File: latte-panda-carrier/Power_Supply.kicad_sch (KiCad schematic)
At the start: 0 parts

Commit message: 110.3
USB-C sub-circuit
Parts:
- added C61: 1uF/16V, A_HDJ_Library:C_0402_1005Metric, symbol Device:C_Small
- added D10, D11: ESD9B5.0ST5G, A_HDJ_Library:D_0402_1005Metric, symbol Diode:ESD9B5.0ST5G
- added D12, D13, D14: D_Zener, A_HDJ_Library:D_0402_1005Metric, symbol Device:D_Zener
- added J17: Barrel_Jack_Switch, symbol Connector:Barrel_Jack_Switch
- added J18: USB_C_Receptacle_USB2.0_16P, symbol Connector:USB_C_Receptacle_USB2.0_16P
- added R36: 10K/1%, A_HDJ_Library:R_0402_1005Metric, symbol Device:R
- added R37: 1K/1%, A_HDJ_Library:R_0402_1005Metric, symbol Device:R
- added R43: 56K/1%, A_HDJ_Library:R_0402_1005Metric, symbol Device:R
- added U14: USB PD等快充协议受电芯片-CH224K-ESSOP10, A_HDJ_Library:ESSOP-10-1EP_3.9x5mm_P1.0mm_EP3.2x2.3, symbol latte_hdj:CH224K
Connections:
- new net: D13.1 (K), J18.A5 (CC1), U14.7 (CC1)
- new net: R36.2, U14.8 (VBUS)
- new net: C61.2, R37.2, U14.1 (VDD)
- new net: J18.A6 (D+), J18.B6 (D+), U14.4 (DP)
- new net: D10.2 (A2), D11.2 (A2), J18.A7 (D-), J18.B7 (D-), U14.5 (DM)
- new net: D14.1 (K), J18.B5 (CC2), U14.6 (CC2)
- new net: R43.1, U14.9 (CFG1)
- new net +15V: D12.1 (K), J18.A4 (VBUS), J18.A9 (VBUS), J18.B4 (VBUS), J18.B9 (VBUS), R36.1
- new net GND: C61.1, D10.1 (A1), D11.1 (A1), D12.2 (A), D13.2 (A), D14.2 (A), J18.A1 (GND), J18.A12 (GND), J18.B1 (GND), J18.B12 (GND), J18.S1 (SHIELD), R37.1, R43.2, U14.0 (GND)
- no-connect marks 0 -> 5

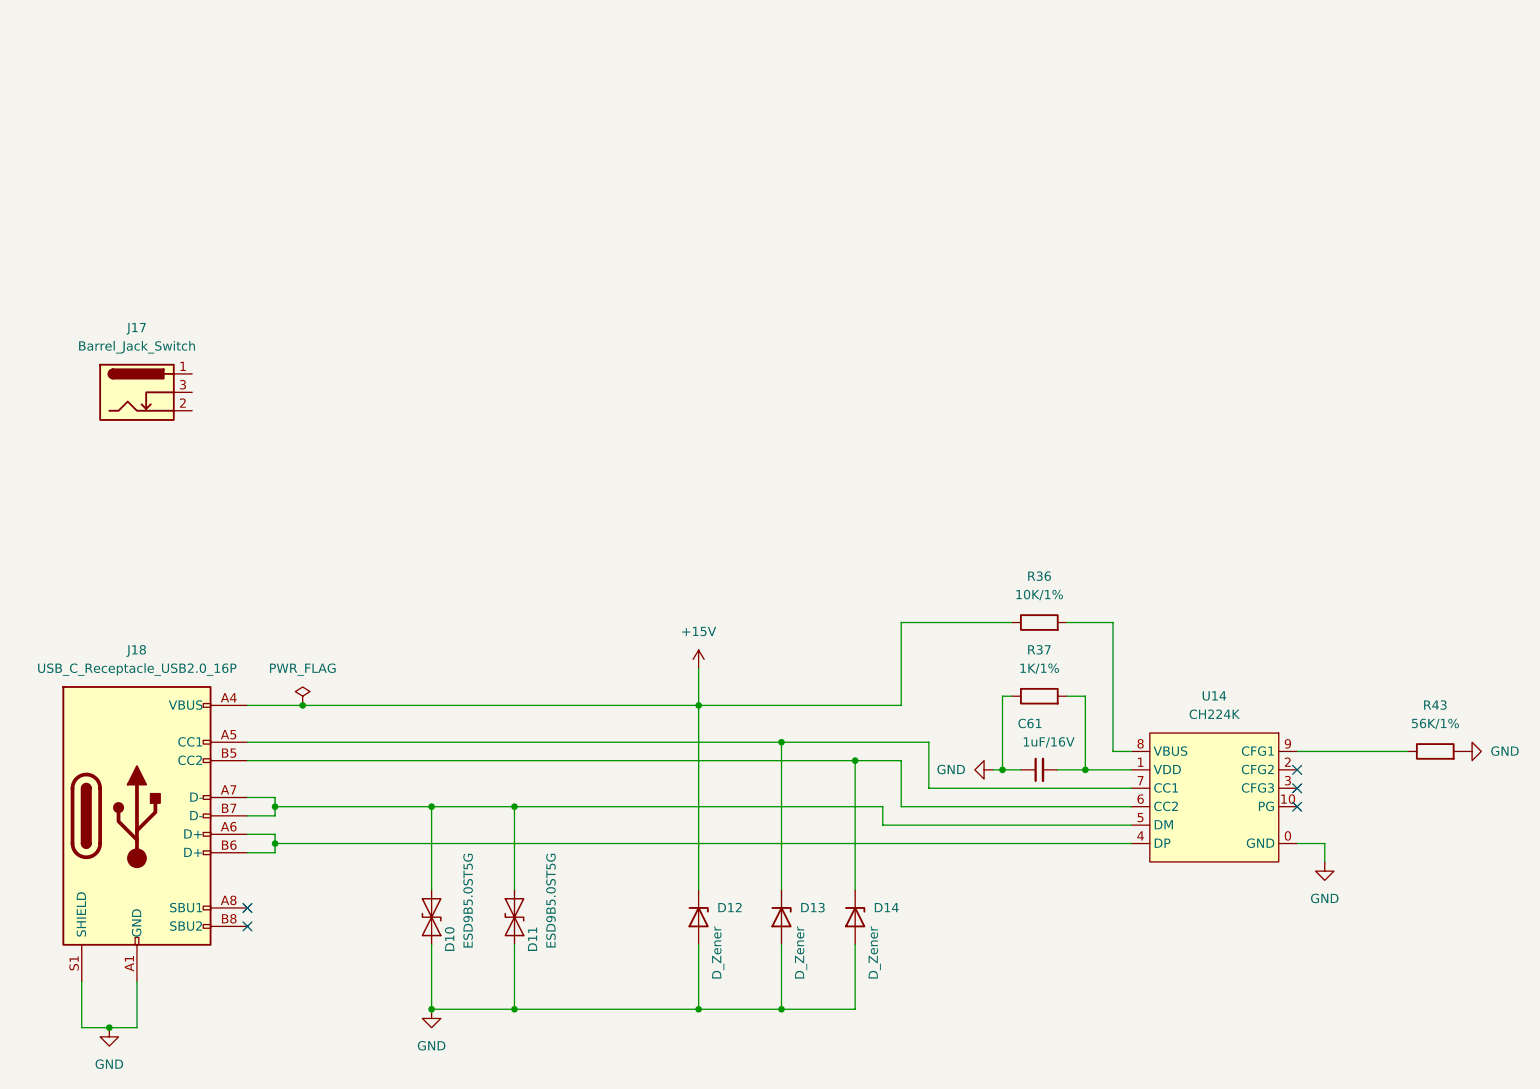
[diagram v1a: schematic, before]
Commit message: 110.3
PSU, Barrel Jack subcircuit
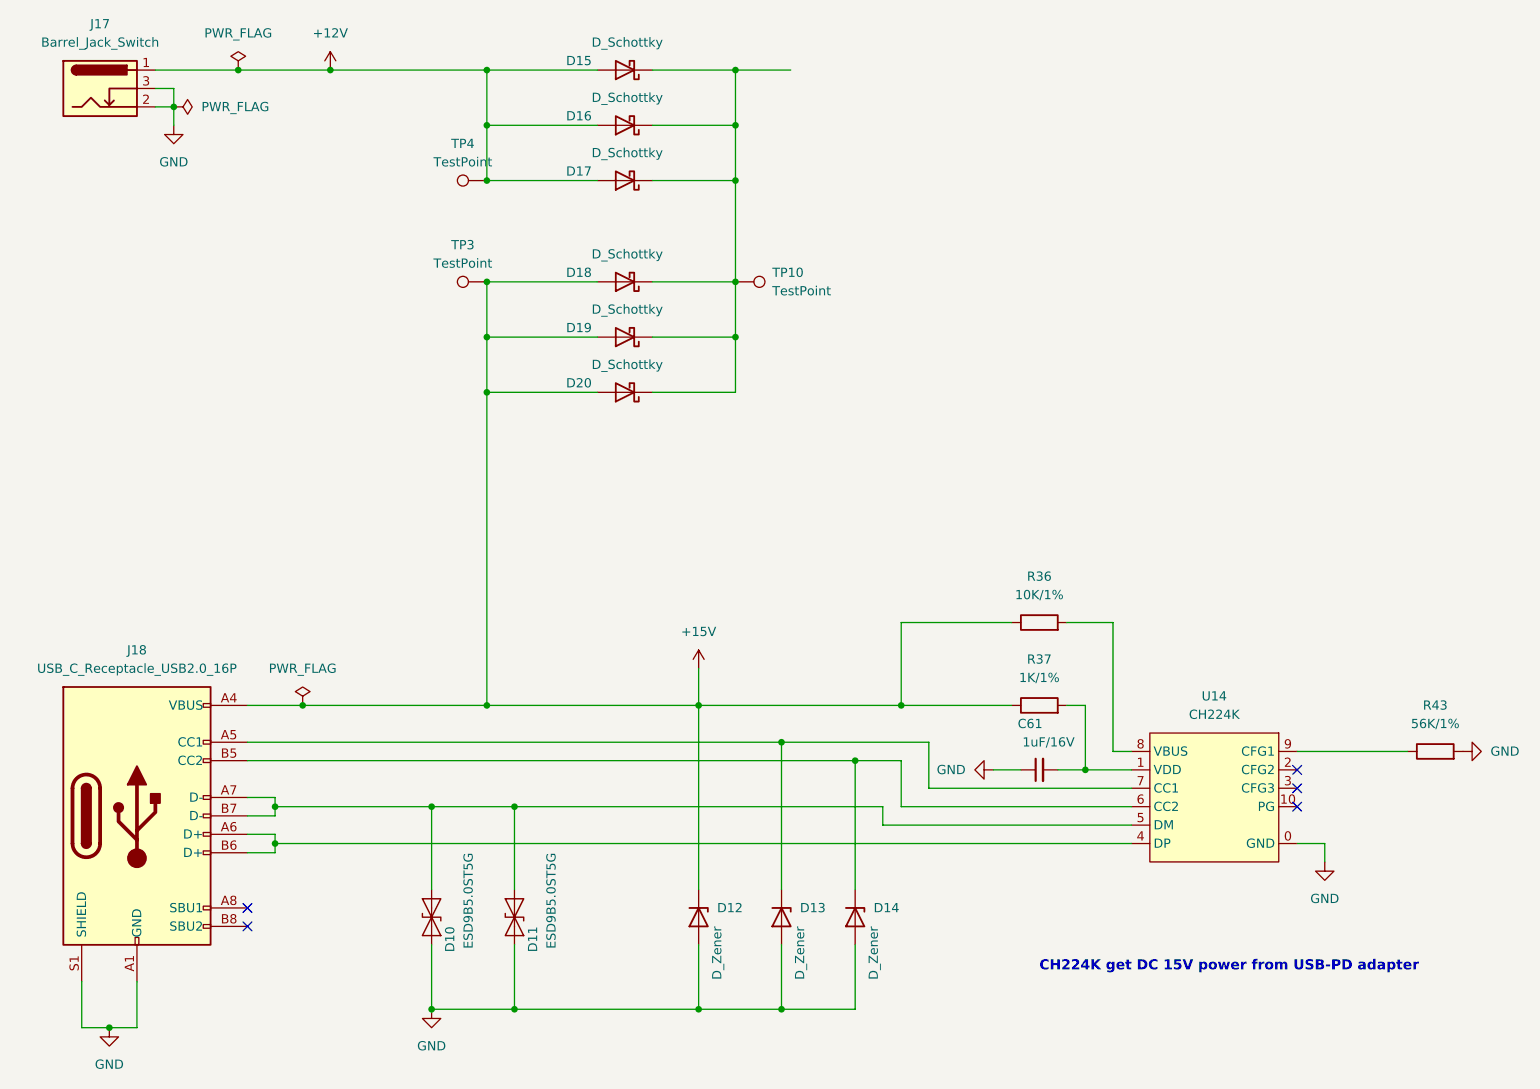
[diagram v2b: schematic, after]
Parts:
- added D15, D16, D17, D18, D19, D20: D_Schottky, A_HDJ_Library:D_SMA, symbol Device:D_Schottky
- added TP10, TP3, TP4: TestPoint, symbol Connector:TestPoint
- J17: footprint (none) -> A_HDJ_Library:DC_Jack_DC007B_30V_10A
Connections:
- net +15V: now also R37.1, D18.2 (A), D19.2 (A), D20.2 (A), TP3.1
- net GND: now also J17.2, J17.3; no longer R37.1
- net +12V: now reaches J17.1
- net +12V: now also D15.2 (A), D16.2 (A), D17.2 (A), TP4.1
- new net: D15.1 (K), D16.1 (K), D17.1 (K), D18.1 (K), D19.1 (K), D20.1 (K), TP10.1
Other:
- note added: "CH224K get DC 15V power from USB-PD adapter"
- moved on the sheet: J17, R37

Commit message: 110.5
PSU, PCIe
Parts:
- added C62: 1uF/16V, A_HDJ_Library:C_0402_1005Metric, symbol Device:C
- added C63: 1uF/16V, A_HDJ_Library:C_0402_1005Metric, symbol Device:C_Small
- added D23: LED, A_HDJ_Library:LED_0603_1608Metric, symbol Device:LED
- added Q5, Q6: 2N7002, A_HDJ_Library:SOT-23, symbol Transistor_FET:2N7002
- added Q7: AON7262E, A_HDJ_Library:MOSFET_PDFN8_3.3x3.3, symbol latte_hdj:AON7262E
- added R38, R40: 10K/1%, A_HDJ_Library:R_0402_1005Metric, symbol Device:R
- added R41, R42, R54: 21.5K/1%, A_HDJ_Library:R_0402_1005Metric, symbol Device:R
- added R44, R45: 100K/1%, A_HDJ_Library:R_0402_1005Metric, symbol Device:R
- added R?: 2.2K/1%, A_HDJ_Library:R_0402_1005Metric, symbol Device:R
- added TP8: TestPoint, symbol Connector:TestPoint
- added U13: TL431DBZ, A_HDJ_Library:SOT-23, symbol Reference_Voltage:TL431DBZ
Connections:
- net +12V: now also C63.1, Q7.1 (S_1), Q7.10 (D_6), Q7.11 (D_7), Q7.2 (S_2), Q7.3 (S_3), Q7.5 (D_1), Q7.6 (D_2), Q7.7 (D_3), Q7.8 (D_4), Q7.9 (D_5), R38.2, R40.2, R44.1, R54.1, TP8.1
- net GND: now also C62.2, D23.1 (K), Q6.2 (S), R42.1, R?.1, U13.3 (A)
- new net: C62.1, Q5.1 (G), R41.1, R42.2
- new net: R40.1, R41.2, U13.1 (K)
- new net: C63.2, Q7.4 (G), R44.2, R45.2
- new net: Q5.2 (S), Q6.3 (D)
- new net: Q5.3 (D), R45.1
- new net: R38.1, R?.2, U13.2 (REF)
- new net: D23.2 (A), R54.2
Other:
- note added: "Power for PCIe x4 OVP@13.86V"
- note added: "soft start"

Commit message: 110.5
PSU, 5V and 3.3V outputs
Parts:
- added C64, C? (x3): 22uF/10V, A_HDJ_Library:C_0402_1005Metric, symbol Device:C_Small
- added C70, C71, C74, C75, C76, C77, C78, C79, C80, C81, C82, C83: 100nF/50V, A_HDJ_Library:C_0603_1608Metric, symbol Device:C_Small
- added C72, C73: 12pF/50V, A_HDJ_Library:C_0402_1005Metric, symbol Device:C_Small
- added D22: LED, A_HDJ_Library:LED_0603_1608Metric, symbol Device:LED
- added D?: 3V3 lzt=5mA, A_HDJ_Library:D_SOD-323, symbol Device:D_Schottky
- added JP1: Jumper_3_Bridged12, symbol Jumper:Jumper_3_Bridged12
- added L1, L2: 2.2uH/4.3A, A_HDJ_Library:L_Sunlord_SWPA4020S, symbol Device:L
- added Q8: 2N7002, A_HDJ_Library:SOT-23, symbol Transistor_FET:2N7002
- added R47: 1K/1%, A_HDJ_Library:R_0402_1005Metric, symbol Device:R
- added R49, R58: 10K/1%, A_HDJ_Library:R_0402_1005Metric, symbol Device:R
- added R51 (x2): 100K/1%, A_HDJ_Library:R_0402_1005Metric, symbol Device:R
- added R52, R53: 2.2K/1%, A_HDJ_Library:R_0402_1005Metric, symbol Device:R
- added R57: 75K/1%, A_HDJ_Library:R_0402_1005Metric, symbol Device:R
- added R59: 21.5K/1%, A_HDJ_Library:R_0402_1005Metric, symbol Device:R
- added R60: 4.7K/1%, A_HDJ_Library:R_0402_1005Metric, symbol Device:R
- added TP5, TP6, TP?: TestPoint, symbol Connector:TestPoint
- added U15, U16: LM2734X, A_HDJ_Library:TSOT-23-6, symbol Regulator_Switching:LM2734X
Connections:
- net GND: now also C64.1, C?.1, C?.2, C?.2, D?.2 (A), Q8.2 (S), R49.2, R51.1, R58.1, R60.1, U15.2 (GND), U16.2 (GND)
- net VDC: now reaches D15.1 (K), D16.1 (K), D17.1 (K), D18.1 (K), D19.1 (K), D20.1 (K), TP10.1
- net VDC: now also C64.2, C?.2, R53.1, U15.5 (VIN), U16.5 (VIN)
- new net: C72.2, C74.2, C76.2, C78.2, C80.2, C82.2, R57.1, R58.2, U15.3 (FB)
- new net: Q8.1 (G), R47.1, R49.1
- new net: D22.1 (K), Q8.3 (D)
- new net: C73.2, C75.2, C77.2, C79.2, C81.2, C83.2, R59.1, R60.2, U16.3 (FB)
- new net: C71.2, U16.1 (BOOST)
- new net: C71.1, L2.1, U16.6 (SW)
- new net: D?.1 (K), R53.2, TP?.1
- new net: D22.2 (A), R52.2
- new net: JP1.2 (C), R51.2
- new net: C70.1, L1.1, U15.6 (SW)
- new net: C70.2, U15.1 (BOOST)
- new net +3.3V: C73.1, C75.1, C77.1, C79.1, C81.1, C83.1, L2.2, R52.1, R59.2, TP6.1
- new net +5V: C72.1, C74.1, C76.1, C78.1, C80.1, C82.1, L1.2, R57.2, TP5.1
- new net PWR_EN: R51.1, R51.2, U15.4 (EN), U16.4 (EN)
- new net SLS_S3: JP1.3 (B)
- new net ~{PWR_LED}/~{PSON}: JP1.1 (A), R47.2
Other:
- note added: "pull-up power for bios_sel"

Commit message: 110.7
PSU, power and reset buttons
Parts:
- added C66, C69: 1uF/16V, A_HDJ_Library:C_0402_1005Metric, symbol Device:C_Small
- added D21, D25: ESD9B5.0ST5G, A_HDJ_Library:D_0402_1005Metric, symbol Diode:ESD9B5.0ST5G
- added R48, R55: 100K/1%, A_HDJ_Library:R_0402_1005Metric, symbol Device:R
- added R50, R56: 10K/1%, A_HDJ_Library:R_0402_1005Metric, symbol Device:R
- added SW1, SW2: SW_Push, A_HDJ_Library:SW_Push_6x6x6, symbol Switch:SW_Push
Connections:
- net +3.3V: now also R50.2, R56.2
- net GND: now also C66.2, C69.2, D21.2 (A2), D25.2 (A2), SW1.1, SW2.2
- new net: C69.1, D25.1 (A1), R55.2, R56.1, SW2.1
- new net: C66.1, D21.1 (A1), R48.2, R50.1, SW1.2
- new net ~{PWR_SW}: R48.1
- new net ~{RST_SW}: R55.1
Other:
- note added: "12V DC input (12V 6A-10A)"
- note added: "15V PD input"
- note added: "LattePanda has integrated pull-up resistors"
- note added: "SY8253ADC 23V 3A 500kHz"
- note added: "Vout = 0.6*(21.5+4.7)/4.7 = 3.446V"
- note added: "Vout = 0.6*(75+10)/10 = 5.1V"

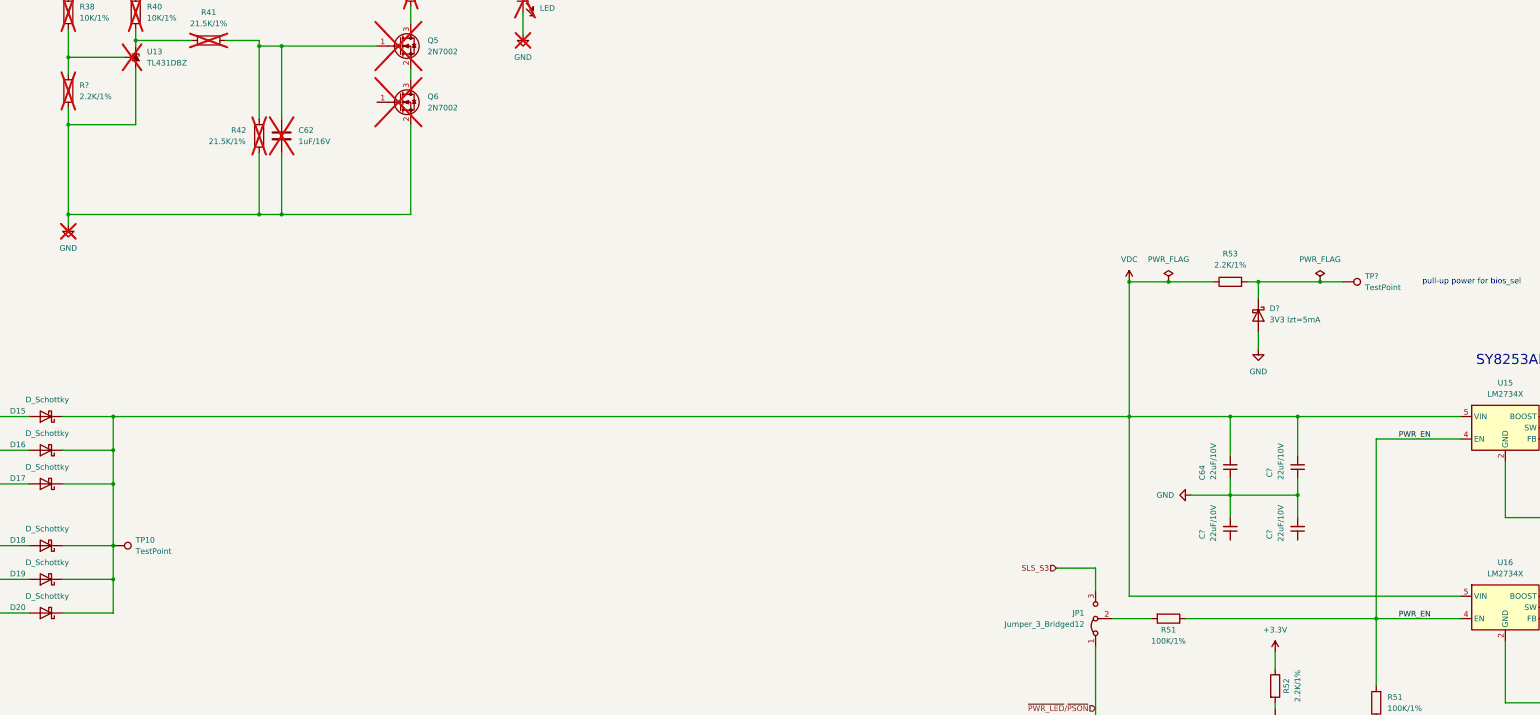
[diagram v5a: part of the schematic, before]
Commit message: Fix missing labels and a few wires
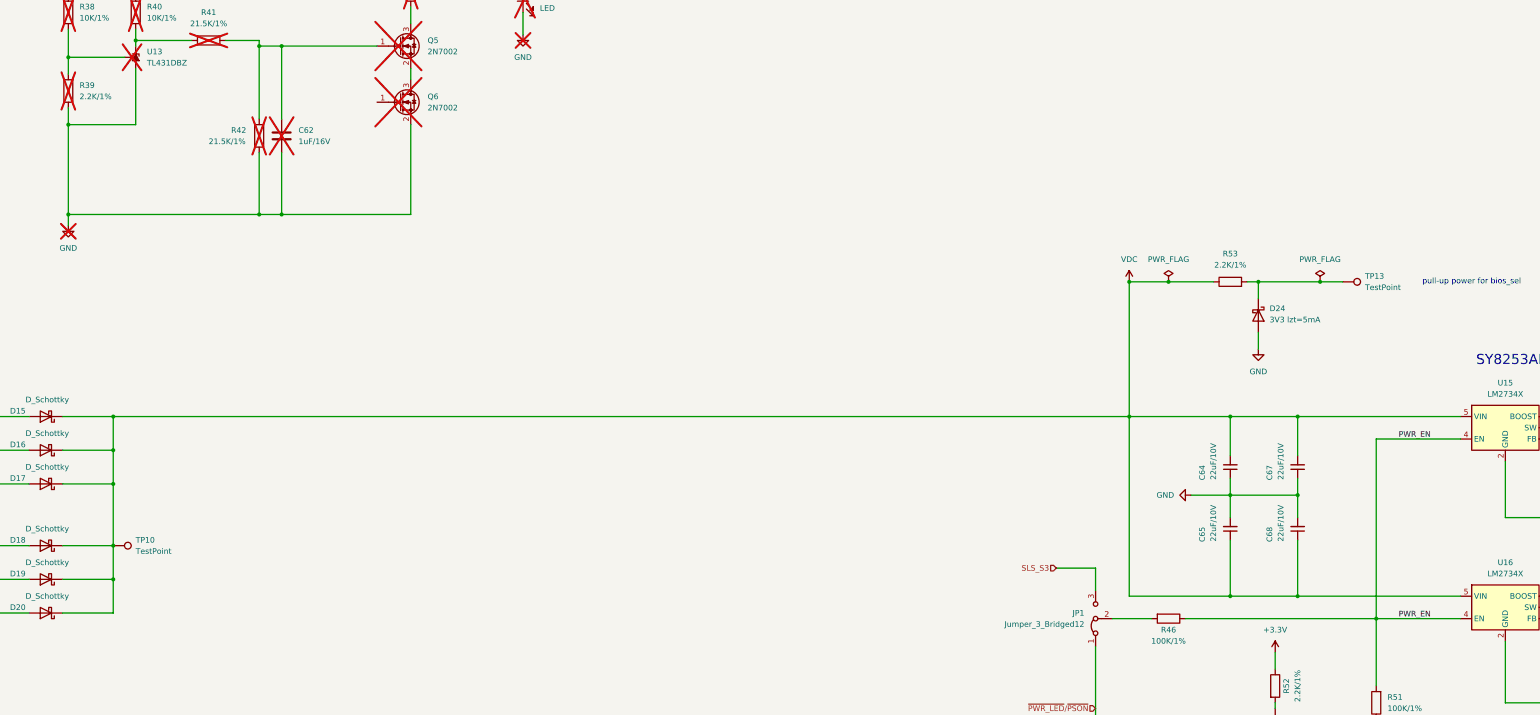
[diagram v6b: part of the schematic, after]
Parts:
- gave numbers to parts that had none: 6
- renumbered R51 to R46
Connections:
- net VDC: now also C65.1, C68.1
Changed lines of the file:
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@@
 	)
 	(junction
+		(at 403.86 226.06)
+		(diameter 0)
+		(color 0 0 0 0)
+	)
+	(junction
 		(at 156.21 85.09)
 		(diameter 0)
@@
 	)
 	(junction
+		(at 419.1 226.06)
+		(diameter 0)
+		(color 0 0 0 0)
+	)
+	(junction
 		(at 95.25 185.42)
 		(diameter 0)
@@
 	(wire
 		(pts
+			(xy 419.1 226.06) (xy 455.93 226.06)
+		)
+		(stroke
+			(width 0)
+			(type default)
+		)
+	)
+	(wire
+		(pts
 			(xy 218.44 106.68) (xy 218.44 109.22)
 		)
@@
 	(wire
 		(pts
-			(xy 381 226.06) (xy 455.93 226.06)
+			(xy 381 226.06) (xy 403.86 226.06)
 		)
 		(stroke
@@
 	(wire
 		(pts
+			(xy 403.86 213.36) (xy 403.86 226.06)
+		)
+		(stroke
+			(width 0)
+			(type default)
+		)
+	)
+	(wire
+		(pts
 			(xy 83.82 278.13) (xy 157.48 278.13)
 		)
@@
 	(wire
 		(pts
+			(xy 419.1 213.36) (xy 419.1 226.06)
+		)
+		(stroke
+			(width 0)
+			(type default)
+		)
+	)
+	(wire
+		(pts
 			(xy 414.02 250.19) (xy 414.02 251.46)
 		)
@@
 	(wire
 		(pts
+			(xy 403.86 226.06) (xy 419.1 226.06)
+		)
+		(stroke
+			(width 0)
+			(type default)
+		)
+	)
+	(wire
+		(pts
 			(xy 547.37 238.76) (xy 539.75 238.76)
 		)
@@
 		(on_board yes)
 		(dnp no)
-		(property "Reference" "R51"
+		(property "Reference" "R46"
 			(at 389.89 233.68 90)
 			(effects
@@
 			(project "latte-panda-carrier"
 				(path "/9ba2df7d-1c0f-41ea-bb38-2c3f31e14521/723302d9-c268-402b-9d89-874b935c2b0c"
-					(reference "R51")
+					(reference "R46")
 					(unit 1)
 				)
@@
 		(dnp no)
 		(fields_autoplaced yes)
-		(property "Reference" "D?"
+		(property "Reference" "D24"
 			(at 412.75 160.9724 90)
 			(effects
@@
 			(project ""
 				(path "/9ba2df7d-1c0f-41ea-bb38-2c3f31e14521/723302d9-c268-402b-9d89-874b935c2b0c"
-					(reference "D?")
+					(reference "D24")
 					(unit 1)
 				)
@@
 		(dnp yes)
 		(fields_autoplaced yes)
-		(property "Reference" "R?"
+		(property "Reference" "R39"
 			(at 143.51 110.4899 0)
 			(effects
@@
 			(project "latte-panda-carrier"
 				(path "/9ba2df7d-1c0f-41ea-bb38-2c3f31e14521/723302d9-c268-402b-9d89-874b935c2b0c"
-					(reference "R?")
+					(reference "R39")
 					(unit 1)
 				)
@@
 		(on_board yes)
 		(dnp no)
-		(property "Reference" "C?"
+		(property "Reference" "C68"
 			(at 412.75 212.09 90)
 			(effects
@@
 			(project "latte-panda-carrier"
 				(path "/9ba2df7d-1c0f-41ea-bb38-2c3f31e14521/723302d9-c268-402b-9d89-874b935c2b0c"
-					(reference "C?")
+					(reference "C68")
 					(unit 1)
 				)
@@
 		(on_board yes)
 		(dnp no)
-		(property "Reference" "C?"
+		(property "Reference" "C65"
 			(at 397.51 212.09 90)
 			(effects
@@
 			(project "latte-panda-carrier"
 				(path "/9ba2df7d-1c0f-41ea-bb38-2c3f31e14521/723302d9-c268-402b-9d89-874b935c2b0c"
-					(reference "C?")
+					(reference "C65")
 					(unit 1)
 				)
@@
 		(dnp no)
 		(fields_autoplaced yes)
-		(property "Reference" "TP?"
+		(property "Reference" "TP13"
 			(at 434.34 153.6699 90)
 			(effects
@@
 			(project ""
 				(path "/9ba2df7d-1c0f-41ea-bb38-2c3f31e14521/723302d9-c268-402b-9d89-874b935c2b0c"
-					(reference "TP?")
+					(reference "TP13")
 					(unit 1)
 				)
@@
 		(on_board yes)
 		(dnp no)
-		(property "Reference" "C?"
+		(property "Reference" "C67"
 			(at 412.75 198.12 90)
 			(effects
@@
 			(project "latte-panda-carrier"
 				(path "/9ba2df7d-1c0f-41ea-bb38-2c3f31e14521/723302d9-c268-402b-9d89-874b935c2b0c"
-					(reference "C?")
+					(reference "C67")
 					(unit 1)
 				)

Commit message: Connected sheet pins for PSU through root sheet
Changed not connected pin errors to warnings and also cleared rest of the
errors.
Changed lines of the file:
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@@
 	)
 	(hierarchical_label "~{RST_SW}"
-		(shape input)
+		(shape output)
 		(at 332.74 307.34 180)
 		(effects
@@
 	)
 	(hierarchical_label "~{PWR_SW}"
-		(shape input)
+		(shape output)
 		(at 270.51 302.26 180)
 		(effects
